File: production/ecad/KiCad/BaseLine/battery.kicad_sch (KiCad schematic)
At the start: 40 parts, among them IC1 AP7362-33SP-13 (3.3V LDO), J14 Power_to_Loadcell, J3 Conn_01x02, J7 Conn_01x07_Pin, Q4 AO3400A, Q5 AO3400A, Q6 AO3400A, U5 LTC3872ETS8TRMPBF

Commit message: Changed 0 ohm to DNP
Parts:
- R45, R46: value 0 -> DNP
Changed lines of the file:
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@@
 			)
 		)
-		(property "Value" "0"
+		(property "Value" "DNP"
 			(at 97.79 48.2599 0)
 			(effects
@@
 			)
 		)
-		(property "Value" "0"
+		(property "Value" "DNP"
 			(at 97.79 39.3699 0)
 			(effects

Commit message: Test point footprints changed
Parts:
- TP10, TP11, TP13: footprint TestPoint:TestPoint_Pad_D1.5mm -> TestPoint:TestPoint_Pad_2.0x2.0mm
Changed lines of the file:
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@@
 			)
 		)
-		(property "Footprint" "TestPoint:TestPoint_Pad_D1.5mm"
+		(property "Footprint" "TestPoint:TestPoint_Pad_2.0x2.0mm"
 			(at 72.39 71.12 0)
 			(effects
@@
 			)
 		)
-		(property "Footprint" "TestPoint:TestPoint_Pad_D1.5mm"
+		(property "Footprint" "TestPoint:TestPoint_Pad_2.0x2.0mm"
 			(at 40.64 50.8 0)
 			(effects
@@
 			)
 		)
-		(property "Footprint" "TestPoint:TestPoint_Pad_D1.5mm"
+		(property "Footprint" "TestPoint:TestPoint_Pad_2.0x2.0mm"
 			(at 146.05 92.71 0)
 			(effects

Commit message: Updated footprint for LDO
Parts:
- IC1: footprint SOIC127P600X150-9N -> SOIC127P600X163-9N 2:SOIC127P600X163-9N
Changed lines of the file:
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@@
 			)
 		)
-		(property "Footprint" "SOIC127P600X150-9N"
+		(property "Footprint" "SOIC127P600X163-9N 2:SOIC127P600X163-9N"
 			(at 83.82 138.1 0)
 			(effects

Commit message: Added fuse footprint
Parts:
- F1, F2: footprint MF-PSML125_6-2:FUSE_MF-PSML125_6-2 -> MF-PSML125_6-2-2:FUSE_MF-PSML125_6-2
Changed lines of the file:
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@@
 			)
 		)
-		(property "Footprint" "MF-PSML125_6-2:FUSE_MF-PSML125_6-2"
+		(property "Footprint" "MF-PSML125_6-2-2:FUSE_MF-PSML125_6-2"
 			(at 133.35 50.8 0)
 			(effects
@@
 			)
 		)
-		(property "Footprint" "MF-PSML125_6-2:FUSE_MF-PSML125_6-2"
+		(property "Footprint" "MF-PSML125_6-2-2:FUSE_MF-PSML125_6-2"
 			(at 146.05 90.17 0)
 			(effects

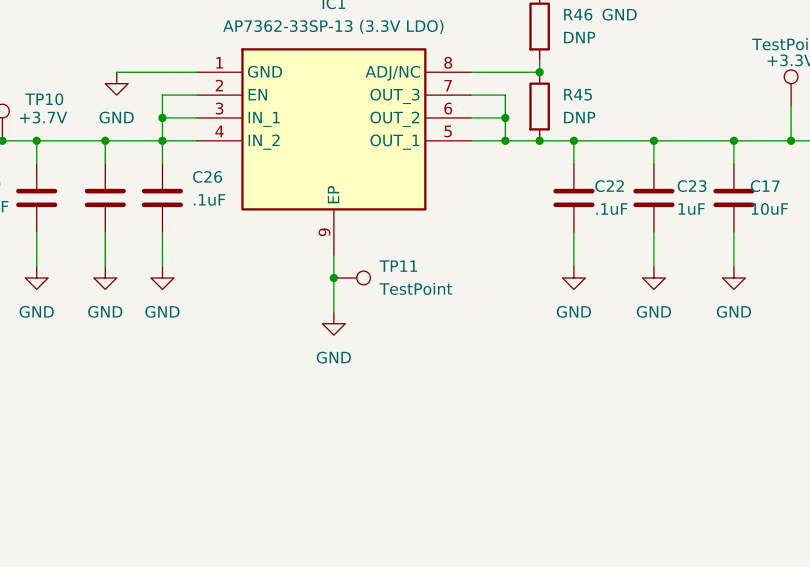
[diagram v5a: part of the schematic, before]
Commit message: fixed schottkey diode footprint
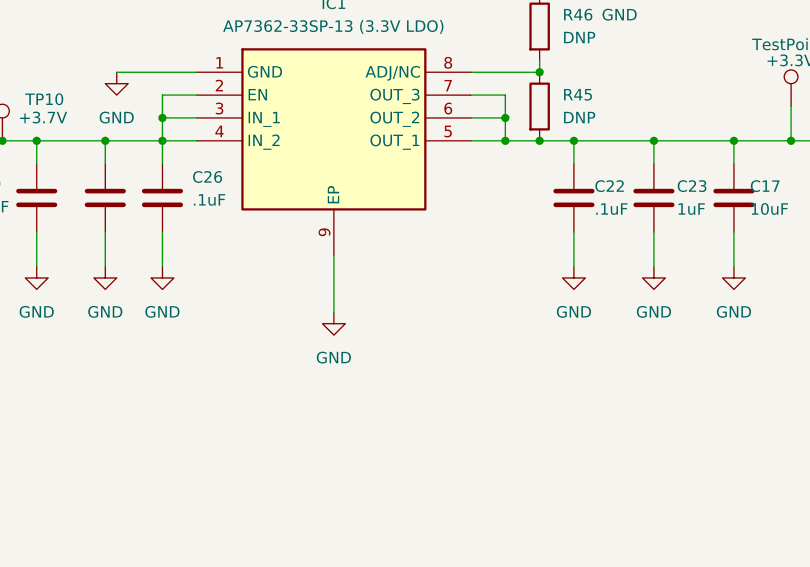
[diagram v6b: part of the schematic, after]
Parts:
- removed TP11: TestPoint, TestPoint:TestPoint_Pad_2.0x2.0mm, symbol Connector:TestPoint
- D2: footprint Diode_SMD:D_0805_2012Metric_Pad1.15x1.40mm_HandSolder -> schotkey:DO-41_STM
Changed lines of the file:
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@@
-	)
-	(junction
-		(at 72.39 66.04)
-		(diameter 0)
-		(color 0 0 0 0)
 	)
 	(junction
@@
 	(wire
 		(pts
-			(xy 72.39 66.04) (xy 72.39 69.85)
+			(xy 72.39 63.5) (xy 72.39 69.85)
 		)
 		(stroke
@@
 		(pts
 			(xy 91.44 50.8) (xy 95.25 50.8)
-		)
-		(stroke
-			(width 0)
-			(type default)
-		)
-	)
-	(wire
-		(pts
-			(xy 72.39 63.5) (xy 72.39 66.04)
 		)
 		(stroke
@@
 	)
 	(symbol
-		(lib_id "Connector:TestPoint")
-		(at 72.39 66.04 270)
-		(unit 1)
-		(exclude_from_sim no)
-		(in_bom yes)
-		(on_board yes)
-		(dnp no)
-		(fields_autoplaced yes)
-		(property "Reference" "TP11"
-			(at 77.47 64.7699 90)
-			(effects
-				(font
-					(size 1.27 1.27)
-				)
-				(justify left)
-			)
-		)
-		(property "Value" "TestPoint"
-			(at 77.47 67.3099 90)
-			(effects
-				(font
-					(size 1.27 1.27)
-				)
-				(justify left)
-			)
-		)
-		(property "Footprint" "TestPoint:TestPoint_Pad_2.0x2.0mm"
-			(at 72.39 71.12 0)
-			(effects
-				(font
-					(size 1.27 1.27)
-				)
-				(hide yes)
-			)
-		)
-		(property "Datasheet" "~"
-			(at 72.39 71.12 0)
-			(effects
-				(font
-					(size 1.27 1.27)
-				)
-				(hide yes)
-			)
-		)
-		(property "Description" "test point"
-			(at 72.39 66.04 0)
-			(effects
-				(font
-					(size 1.27 1.27)
-				)
-				(hide yes)
-			)
-		)
-		(pin "1"
-		)
-		(instances
-			(project "BaseLine"
-				(path "/ba9eda21-3882-41e1-8265-3d8ac781da20/31f727a4-3278-43bf-88f9-c0e8e93f0a52"
-					(reference "TP11")
-					(unit 1)
-				)
-			)
-		)
-	)
-	(symbol
 		(lib_id "power:GND")
 		(at 20.32 33.02 0)
@@
 			)
 		)
-		(property "Footprint" "Diode_SMD:D_0805_2012Metric_Pad1.15x1.40mm_HandSolder"
+		(property "Footprint" "schotkey:DO-41_STM"
 			(at 115.57 124.46 0)
 			(effects

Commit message: add zener diode
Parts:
- D3: footprint Diode_SMD:D_0805_2012Metric_Pad1.15x1.40mm_HandSolder -> zener:DIOAD1165W56L425D185
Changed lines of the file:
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@@
 			)
 		)
-		(property "Footprint" "Diode_SMD:D_0805_2012Metric_Pad1.15x1.40mm_HandSolder"
+		(property "Footprint" "zener:DIOAD1165W56L425D185"
 			(at 151.13 121.92 0)
 			(effects

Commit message: doing some things for layout
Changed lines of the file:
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@@
 		(on_board yes)
 		(dnp no)
-		(fields_autoplaced yes)
 		(property "Reference" "C25"
-			(at 50.8 55.8799 0)
+			(at 50.8 55.88 0)
 			(effects
 				(font
@@
 				)
 				(justify right)
-				(hide yes)
 			)
 		)
